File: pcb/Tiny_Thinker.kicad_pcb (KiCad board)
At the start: 2 copper layers, 47.9 x 46 mm, 35 parts, among them J1 USB_B_Micro, J2 SWD, J3 I2C1_A, J4 I2C1_B, J5 SPI1, J6 PWM_OUT, J7 ADC1, SW1 SW_Push, SW2 SW_SPDT, U1 STM32F446RET6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

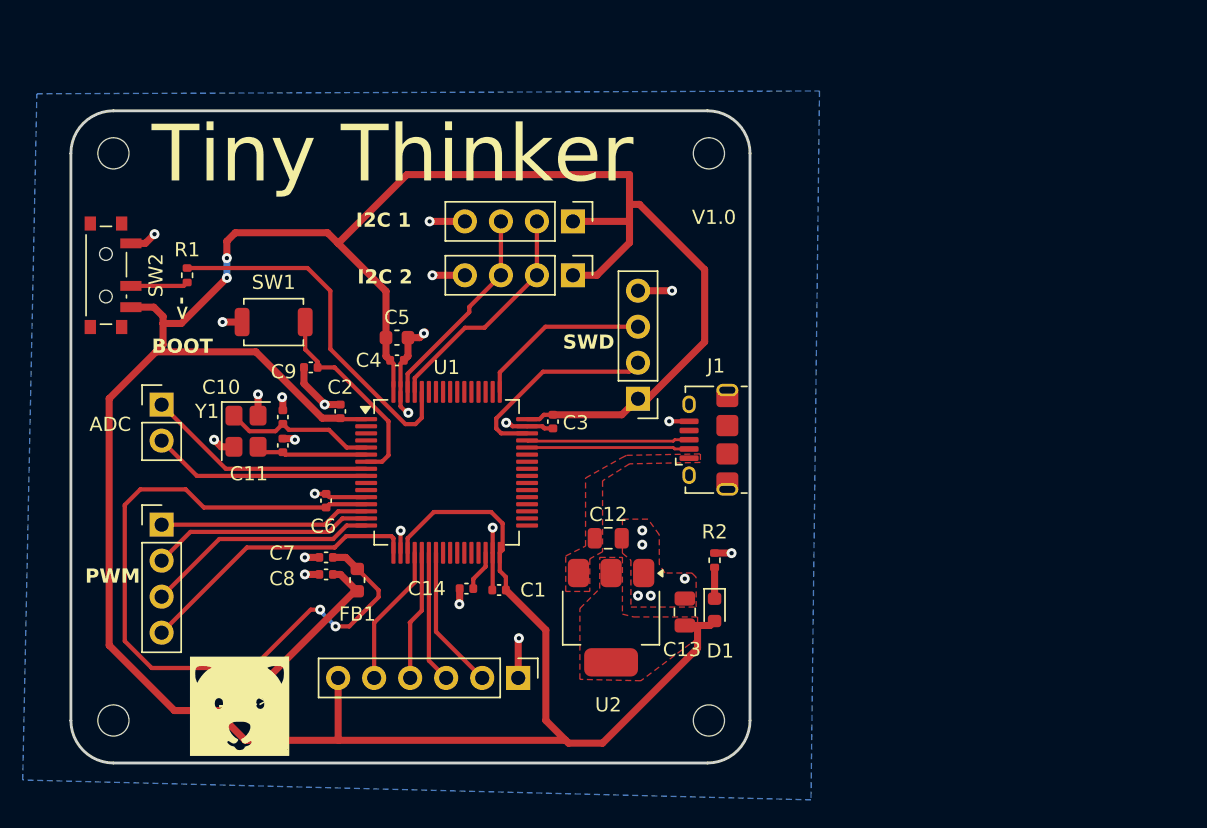
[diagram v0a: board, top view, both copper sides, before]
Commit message: added extra 100nf cap
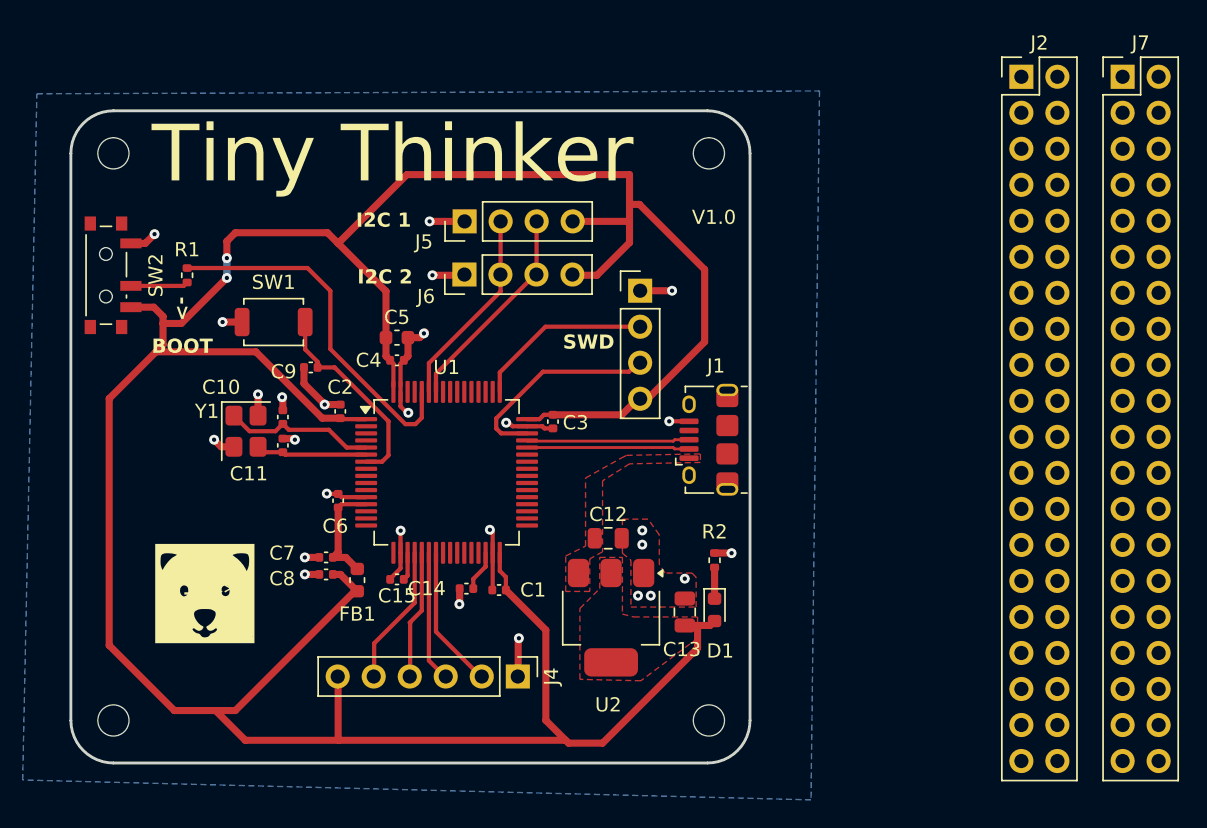
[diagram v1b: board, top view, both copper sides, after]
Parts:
- added C15: 100nF, Capacitor_SMD:C_0402_1005Metric, F.Cu at (105.0, 90.0)
- C1, C2, C3, C4, C9: value 100n -> 100nF
- C10, C11: value 10p -> 10pF
- C12, C13: value 22u -> 22uF
- C14: value 4.7u -> 4.7uF
- C5: value 10u -> 10uF
- C6: value 10n -> 10nF
- C7, C8: value 1u -> 1uF
- J2: value SWD -> Conn_02x20_Odd_Even; footprint Connector_PinHeader_2.54mm:PinHeader_1x04_P2.54mm_Vertical -> Connector_PinHeader_2.54mm:PinHeader_2x20_P2.54mm_Vertical
- J3: value I2C1_A -> SWD
- J4: value I2C1_B -> SPI1; footprint Connector_PinHeader_2.54mm:PinHeader_1x04_P2.54mm_Vertical -> Connector_PinHeader_2.54mm:PinHeader_1x06_P2.54mm_Vertical
- J5: value SPI1 -> I2C1_A; footprint Connector_PinHeader_2.54mm:PinHeader_1x06_P2.54mm_Vertical -> Connector_PinHeader_2.54mm:PinHeader_1x04_P2.54mm_Vertical
- J6: value PWM_OUT -> I2C1_B
- J7: value ADC1 -> Conn_02x20_Odd_Even; footprint Connector_PinHeader_2.54mm:PinHeader_1x02_P2.54mm_Vertical -> Connector_PinHeader_2.54mm:PinHeader_2x20_P2.54mm_Vertical
- moved J7 71.6 mm to (156.2, 54.6)
- moved J2 35.3 mm to (149.0, 54.6), turned to 0 degrees
- moved J5 32.4 mm to (109.8, 64.8), turned to 90 degrees
- moved J4 28.6 mm to (113.5, 96.9)
- moved J6 27.7 mm to (109.8, 68.5), turned to 90 degrees
- moved G*** 8.32 mm to (91.5, 91.0)
- moved J3 6.81 mm to (122.2, 69.7), turned to 0 degrees
- moved C6 0.85 mm to (100.8, 84.5)
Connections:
- J2 pad 1: +3.3V -> GND
- J2 pad 2: /SWDIO -> GND
- J2 pad 3: /SWCLK -> +3.3V
- J2 pad 4: GND -> +3.3V
- J3 pad 1: +3.3V -> GND
- J3 pad 2: /I2C1_SCL -> /SWCLK
- J3 pad 3: /I2C1_SDA -> /SWDIO
- J3 pad 4: GND -> +3.3V
- J4 pad 1: +3.3V -> GND
- J4 pad 2: /I2C1_SCL -> /SPI1_MOSI
- J4 pad 3: /I2C1_SDA -> /SPI1_MISO
- J4 pad 4: GND -> /SPI1_SCK
- J5 pad 2: /SPI1_MOSI -> /I2C1_SDA
- J5 pad 3: /SPI1_MISO -> /I2C1_SCL
- J5 pad 4: /SPI1_SCK -> +3.3V
- J6 pad 1: /PWM_1 -> GND
- J6 pad 2: /PWM_2 -> /I2C1_SDA
- J6 pad 3: /PWM_3 -> /I2C1_SCL
- J6 pad 4: /PWM_4 -> +3.3V
- J7 pad 1: /ADC_1 -> GND
- J7 pad 2: /ADC_2 -> GND
- U1 pad 10: unconnected-(U1-PC2-Pad10) -> /PC2
- U1 pad 11: unconnected-(U1-PC3-Pad11) -> /PC3
- U1 pad 14: /PWM_1 -> /PA0
- U1 pad 15: /PWM_2 -> /PA1
- U1 pad 16: /PWM_3 -> /PA2
- U1 pad 17: /PWM_4 -> /PA3
- U1 pad 2: unconnected-(U1-PC13-Pad2) -> /PC13
- U1 pad 24: unconnected-(U1-PC4-Pad24) -> /PC4
- U1 pad 25: unconnected-(U1-PC5-Pad25) -> /PC5
- U1 pad 26: unconnected-(U1-PB0-Pad26) -> /PB0
- U1 pad 27: unconnected-(U1-PB1-Pad27) -> /PB1
- U1 pad 28: unconnected-(U1-PB2-Pad28) -> /PB2
- U1 pad 29: unconnected-(U1-PB10-Pad29) -> /PB10
- U1 pad 3: unconnected-(U1-PC14-Pad3) -> /PC14
- U1 pad 33: unconnected-(U1-PB12-Pad33) -> /PB12
- U1 pad 34: unconnected-(U1-PB13-Pad34) -> /PB13
- U1 pad 35: unconnected-(U1-PB14-Pad35) -> /PB14
- U1 pad 36: unconnected-(U1-PB15-Pad36) -> /PB15
- U1 pad 37: unconnected-(U1-PC6-Pad37) -> /PC6
- U1 pad 38: unconnected-(U1-PC7-Pad38) -> /PC7
- U1 pad 39: unconnected-(U1-PC8-Pad39) -> /PC8
- U1 pad 4: unconnected-(U1-PC15-Pad4) -> /PC15
- U1 pad 40: unconnected-(U1-PC9-Pad40) -> /PC9
- U1 pad 41: unconnected-(U1-PA8-Pad41) -> /PA8
- U1 pad 42: unconnected-(U1-PA9-Pad42) -> /PA9
- U1 pad 43: unconnected-(U1-PA10-Pad43) -> /PA10
- U1 pad 50: unconnected-(U1-PA15-Pad50) -> /PA15
- U1 pad 51: unconnected-(U1-PC10-Pad51) -> /PC10
- U1 pad 52: unconnected-(U1-PC11-Pad52) -> /PC11
- U1 pad 53: unconnected-(U1-PC12-Pad53) -> /PC12
- U1 pad 54: unconnected-(U1-PD2-Pad54) -> /PD2
- U1 pad 55: unconnected-(U1-PB3-Pad55) -> /PB3
- U1 pad 56: unconnected-(U1-PB4-Pad56) -> /PB4
- U1 pad 57: unconnected-(U1-PB5-Pad57) -> /PB5
- U1 pad 58: unconnected-(U1-PB6-Pad58) -> /I2C1_SCL
- U1 pad 59: unconnected-(U1-PB7-Pad59) -> /I2C1_SDA
- U1 pad 61: /I2C1_SCL -> /PB8
- U1 pad 62: /I2C1_SDA -> /PB9
- U1 pad 8: /ADC_1 -> /PC0
- U1 pad 9: /ADC_2 -> /PC1
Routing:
- net +3.3VA: track 54.2 -> 7.80 mm, vias 2 -> 0
- net /PWM_4: track 20.3 -> 0.00 mm
- net /PWM_3: track 16.5 -> 0.00 mm
- net /ADC_1: track 16.3 -> 0.00 mm
- net /PWM_2: track 15.7 -> 0.00 mm
- net /ADC_2: track 15.5 -> 0.00 mm
- net /PWM_1: track 14.8 -> 0.00 mm
- net +3.3V: track 233.2 -> 224.2 mm
- net /I2C1_SCL: track 16.4 -> 15.0 mm
- net GND: track 48.3 -> 49.4 mm
- net /I2C1_SDA: track 14.8 -> 14.1 mm
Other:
- board text removed: "ADC"
- board text removed: "ADC 1"
- board text removed: "ADC 2"
- board text removed: "PWM"
- board text removed: "PWM 1"
- board text removed: "PWM 2"
- board text removed: "PWM 3"
- board text removed: "PWM 4"

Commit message: I honestly forgot what I did
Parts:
- moved C10 2.49 mm to (98.8, 80.3)
- moved C11 2.49 mm to (98.8, 82.3)
- moved Y1 2.49 mm to (96.2, 81.3)
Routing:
- net +3.3V: track 224.2 -> 228.0 mm, vias 2 -> 0
- net /HSE_IN: track 10.7 -> 8.14 mm
- net /HSE_OUT: track 7.85 -> 6.54 mm
- net GND: track 49.4 -> 48.7 mm, vias 27 -> 30
- net /BOOT0: vias 0 -> 2
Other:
- board text added: "I2C1 A"
- board text added: "I2C1 B"
- board text removed: "I2C 1"
- board text removed: "I2C 2"

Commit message: i dont even know
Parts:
- removed G***: LOGO, LOGO
- added R3: 4k7, Resistor_SMD:R_0402_1005Metric, F.Cu at (120.9, 81.9)
- added R4: 10k, Resistor_SMD:R_0402_1005Metric, F.Cu at (118.9, 82.2)
- moved J2 86.3 mm to (80.9, 107.5), turned to 90 degrees
- moved H4 76.3 mm to (155.2, 70.1)
- moved J7 74.5 mm to (81.7, 57.7), turned to 90 degrees
- moved H3 70.3 mm to (155.2, 64.2)
- moved J6 54.4 mm to (163.7, 75.4), turned to 0 degrees
- moved J5 50.5 mm to (159.1, 75.4), turned to 0 degrees
- moved H2 50.4 mm to (155.2, 58.2)
- moved H1 29.2 mm to (155.2, 52.3)
- moved J3 5.57 mm to (116.8, 71.2), turned to 90 degrees
- moved J4 2.09 mm to (114.0, 99.0)
- moved J1 1.50 mm to (125.5, 80.2)
- moved C1 0.80 mm to (112.2, 90.0)
- moved C14 0.70 mm to (109.9, 90.0)
- moved C3 0.41 mm to (115.8, 78.6)
- moved C12 0.40 mm to (119.5, 87.2)
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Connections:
- U1 pad 10: /PC2 -> /ADC1_IN12
- U1 pad 11: /PC3 -> /ADC1_IN13
- U1 pad 14: /PA0 -> unconnected-(U1-PA0-Pad14)
- U1 pad 15: /PA1 -> unconnected-(U1-PA1-Pad15)
- U1 pad 16: /PA2 -> unconnected-(U1-PA2-Pad16)
- U1 pad 17: /PA3 -> unconnected-(U1-PA3-Pad17)
- U1 pad 2: /PC13 -> unconnected-(U1-PC13-Pad2)
- U1 pad 24: /PC4 -> /ADC1_IN14
- U1 pad 25: /PC5 -> /ADC1_IN15
- U1 pad 26: /PB0 -> /ADC1_IN8
- U1 pad 27: /PB1 -> /ADC1_IN9
- U1 pad 28: /PB2 -> /TIM2_CH4
- U1 pad 29: /PB10 -> /TIM2_CH3
- U1 pad 3: /PC14 -> unconnected-(U1-PC14-Pad3)
- U1 pad 33: /PB12 -> unconnected-(U1-PB12-Pad33)
- U1 pad 34: /PB13 -> unconnected-(U1-PB13-Pad34)
- U1 pad 35: /PB14 -> unconnected-(U1-PB14-Pad35)
- U1 pad 36: /PB15 -> unconnected-(U1-PB15-Pad36)
- U1 pad 37: /PC6 -> unconnected-(U1-PC6-Pad37)
- U1 pad 38: /PC7 -> unconnected-(U1-PC7-Pad38)
- U1 pad 39: /PC8 -> /TIM3_CH3
- U1 pad 4: /PC15 -> unconnected-(U1-PC15-Pad4)
- U1 pad 40: /PC9 -> /TIM3_CH4
- U1 pad 41: /PA8 -> unconnected-(U1-PA8-Pad41)
- U1 pad 42: /PA9 -> /USB_VBUS
- U1 pad 43: /PA10 -> unconnected-(U1-PA10-Pad43)
- U1 pad 50: /PA15 -> /TIM2_CH1
- U1 pad 51: /PC10 -> unconnected-(U1-PC10-Pad51)
- U1 pad 52: /PC11 -> unconnected-(U1-PC11-Pad52)
- U1 pad 53: /PC12 -> unconnected-(U1-PC12-Pad53)
- U1 pad 54: /PD2 -> unconnected-(U1-PD2-Pad54)
- U1 pad 55: /PB3 -> /TIM2_CH2
- U1 pad 56: /PB4 -> /TIM3_CH1
- U1 pad 57: /PB5 -> /TIM3_CH2
- U1 pad 61: /PB8 -> /CAN1_RX
- U1 pad 62: /PB9 -> /CAN1_TX
- U1 pad 8: /PC0 -> /ADC1_IN10
- U1 pad 9: /PC1 -> /ADC1_IN11
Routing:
- net +3.3V: track 228.0 -> 204.0 mm
- net /I2C1_SCL: track 15.0 -> 0.00 mm
- net /I2C1_SDA: track 14.1 -> 0.00 mm
- net GND: track 48.7 -> 35.7 mm, vias 30 -> 26
- net /SPI1_MOSI: track 10.2 -> 0.00 mm
- net /SPI1_NSS: track 10.0 -> 0.00 mm
- net /SPI1_MISO: track 9.33 -> 0.00 mm
- net /SPI1_SCK: track 9.19 -> 0.00 mm
- net /USB_VBUS: track 0.00 -> 6.29 mm
- net /USB_D-: track 11.5 -> 9.69 mm
- net /USB_D+: track 11.5 -> 9.74 mm
- net /SWCLK: track 12.5 -> 11.0 mm
- net /SWDIO: track 14.6 -> 13.5 mm
- net /VCAP_1: track 2.89 -> 2.21 mm
- removed copper zone on B.Cu, net GND
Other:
- board outline removed
- board text removed: "+3.3V"
- board text removed: "GND"
- board text removed: "I2C1 A"
- board text removed: "I2C1 B"
- board text removed: "MISO"
- board text removed: "MOSI"
- board text removed: "NSS"
- board text removed: "SCK"
- board text removed: "SCL"
- board text removed: "SDA"
- board text removed: "SWCLK"
- board text removed: "SWD"
- board text removed: "SWDIO"
- board text removed: "Tiny Thinker"
- board text removed: "V1.0"

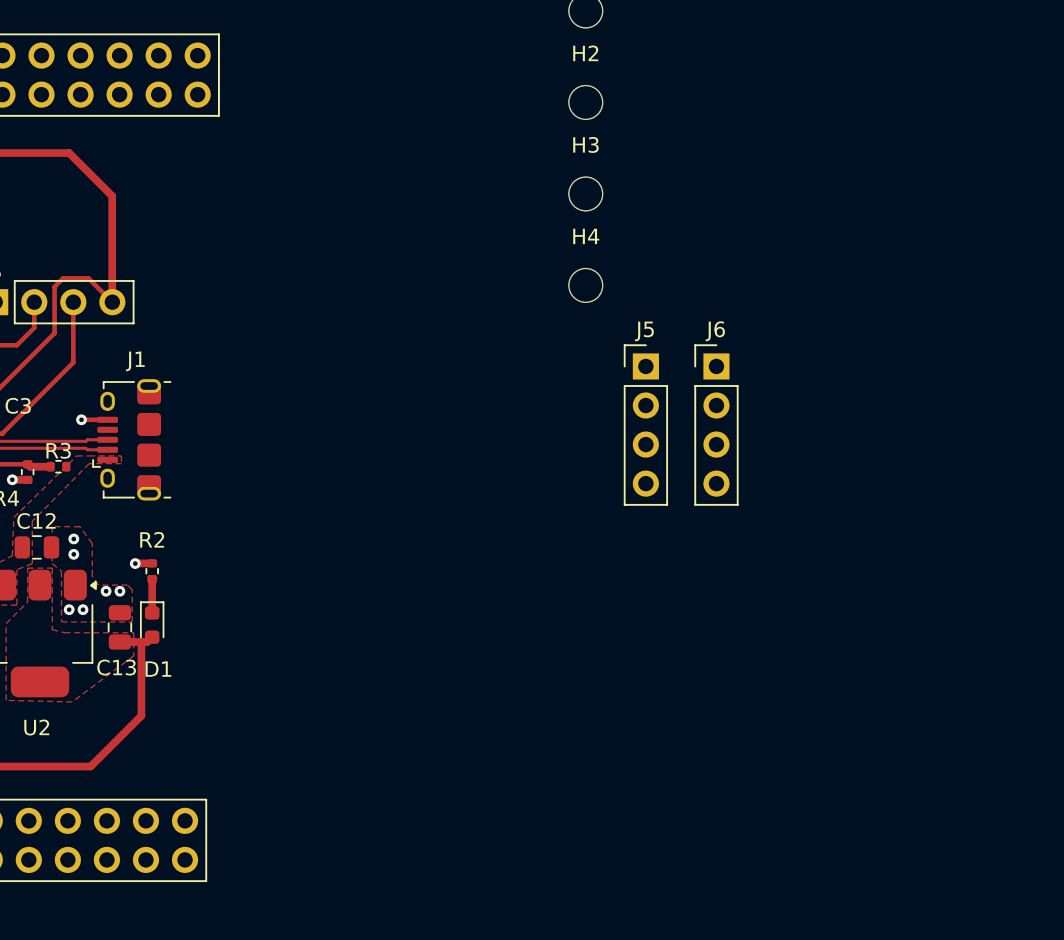
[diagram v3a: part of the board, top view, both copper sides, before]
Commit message: Added JLCPCB capabilities
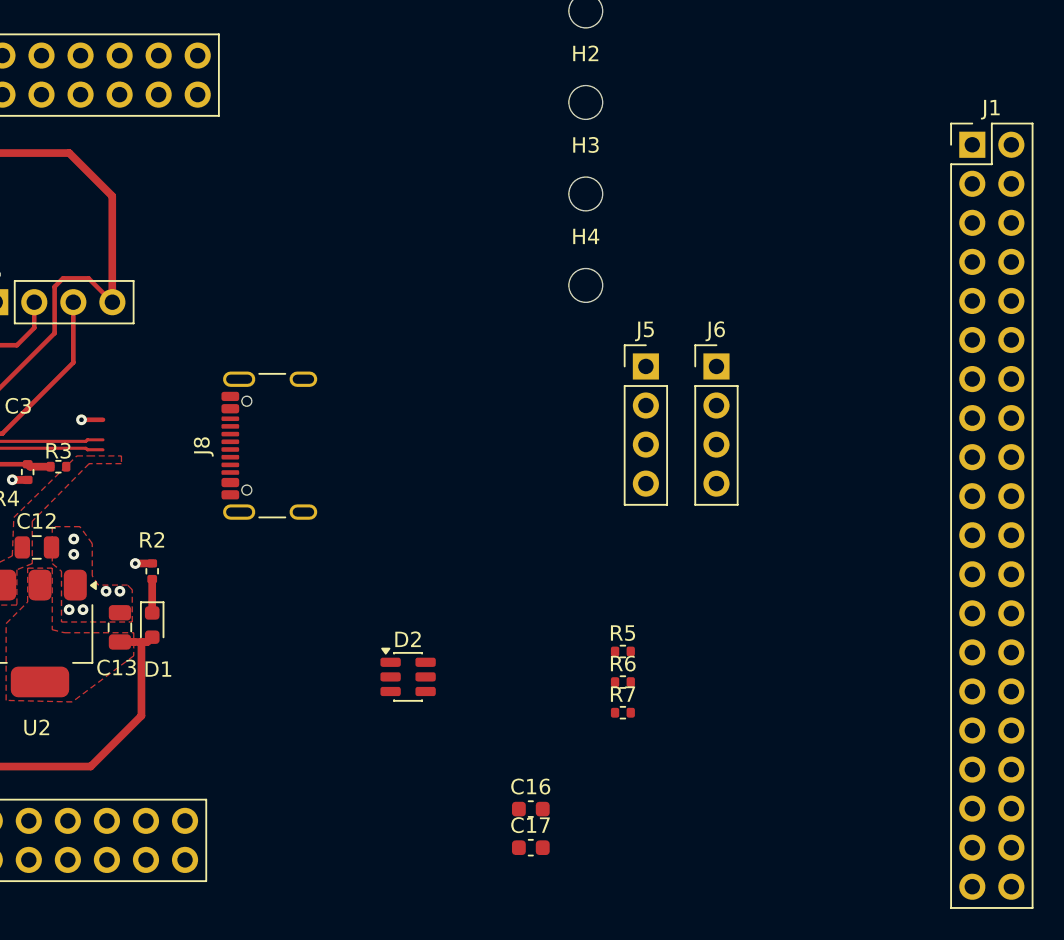
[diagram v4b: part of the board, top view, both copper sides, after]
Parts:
- added C16: 470nF, Capacitor_SMD:C_0603_1608Metric, F.Cu at (151.6, 104.2)
- added C17: 470nF, Capacitor_SMD:C_0603_1608Metric, F.Cu at (151.6, 106.7)
- added D2: USBLC6-2SC6, Package_TO_SOT_SMD:SOT-23-6, F.Cu at (143.6, 95.6)
- added J8: USB_C_Receptacle_USB2.0_16P, Connector_USB:USB_C_Receptacle_GCT_USB4105-xx-A_16P_TopMnt_Horizontal, F.Cu at (135.8, 80.5)
- added R5: 0R, Resistor_SMD:R_0402_1005Metric, F.Cu at (157.6, 93.9)
- added R6: 5k1, Resistor_SMD:R_0402_1005Metric, F.Cu at (157.6, 95.9)
- added R7: 5k1, Resistor_SMD:R_0402_1005Metric, F.Cu at (157.6, 97.9)
- FB1: value FerriteBead -> 120R
- J1: value USB_B_Micro -> Conn_02x20_Odd_Even; footprint Connector_USB:USB_Micro-B_Amphenol_10118194_Horizontal -> Connector_PinHeader_2.54mm:PinHeader_2x20_P2.54mm_Vertical
- moved J1 58.1 mm to (180.3, 61.0), turned to 0 degrees
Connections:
- C12 pad 1: VBUS -> +VBUSF
- J1 pad 1: VBUS -> +3.3V
- J1 pad 2: /USB_D- -> GND
- J1 pad 3: /USB_D+ -> GND
- J1 pad 4: unconnected-(J1-ID-Pad4) -> +3.3V
- J1 pad 5: GND -> unconnected-(J1-Pin_5-Pad5)
- J2 pad 1: GND -> +3.3V
- J2 pad 10: /PA3 -> unconnected-(J2-Pin_10-Pad10)
- J2 pad 11: GND -> unconnected-(J2-Pin_11-Pad11)
- J2 pad 12: GND -> unconnected-(J2-Pin_12-Pad12)
- J2 pad 13: /PA8 -> unconnected-(J2-Pin_13-Pad13)
- J2 pad 14: /PA9 -> GND
- J2 pad 15: /PA10 -> GND
- J2 pad 16: /PA15 -> unconnected-(J2-Pin_16-Pad16)
- J2 pad 17: GND -> unconnected-(J2-Pin_17-Pad17)
- J2 pad 18: GND -> unconnected-(J2-Pin_18-Pad18)
- J2 pad 19: /PB0 -> +3.3V
- J2 pad 20: /PB1 -> GND
- J2 pad 21: /PB2 -> GND
- J2 pad 22: /PB3 -> +3.3V
- J2 pad 23: GND -> unconnected-(J2-Pin_23-Pad23)
- J2 pad 24: GND -> unconnected-(J2-Pin_24-Pad24)
- J2 pad 25: /PB4 -> unconnected-(J2-Pin_25-Pad25)
- J2 pad 26: /PB5 -> GND
- J2 pad 27: /PB8 -> GND
- J2 pad 28: /PB9 -> unconnected-(J2-Pin_28-Pad28)
- J2 pad 29: GND -> unconnected-(J2-Pin_29-Pad29)
- J2 pad 3: +3.3V -> GND
- J2 pad 30: GND -> unconnected-(J2-Pin_30-Pad30)
- J2 pad 31: /PB10 -> unconnected-(J2-Pin_31-Pad31)
- J2 pad 32: /PB12 -> GND
- J2 pad 33: /PB13 -> GND
- J2 pad 34: /PB14 -> unconnected-(J2-Pin_34-Pad34)
- J2 pad 35: GND -> unconnected-(J2-Pin_35-Pad35)
- J2 pad 36: GND -> unconnected-(J2-Pin_36-Pad36)
- J2 pad 37: GND -> +3.3V
- J2 pad 39: +3.3V -> GND
- J2 pad 5: GND -> unconnected-(J2-Pin_5-Pad5)
- J2 pad 6: GND -> unconnected-(J2-Pin_6-Pad6)
- J2 pad 7: /PA0 -> unconnected-(J2-Pin_7-Pad7)
- J2 pad 8: /PA1 -> GND
- J2 pad 9: /PA2 -> GND
- R3 pad 1: VBUS -> +VBUSF
- U1 pad 14: unconnected-(U1-PA0-Pad14) -> /TIM2_CH1
- U1 pad 15: unconnected-(U1-PA1-Pad15) -> /TIM2_CH2
- U1 pad 16: unconnected-(U1-PA2-Pad16) -> /TIM2_CH3
- U1 pad 17: unconnected-(U1-PA3-Pad17) -> /TIM2_CH4
- U1 pad 28: /TIM2_CH4 -> unconnected-(U1-PB2-Pad28)
- U1 pad 29: /TIM2_CH3 -> unconnected-(U1-PB10-Pad29)
- U1 pad 50: /TIM2_CH1 -> unconnected-(U1-PA15-Pad50)
- U1 pad 55: /TIM2_CH2 -> unconnected-(U1-PB3-Pad55)
- U2 pad 3: VBUS -> +VBUSF
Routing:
- added copper zone on F.Cu, net +VBUSF
- removed copper zone on F.Cu, net VBUS
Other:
- copper layers 2 -> 4
- rule pad_to_mask_clearance: 0 -> 0.1

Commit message: checkpoint
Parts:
- added FM1: Fiducial, Fiducial:Fiducial_1mm_Mask2mm, F.Cu at (205.0, 90.9)
- added FM2: Fiducial, Fiducial:Fiducial_1mm_Mask2mm, F.Cu at (205.0, 94.5)
- added FM3: Fiducial, Fiducial:Fiducial_1mm_Mask2mm, F.Cu at (205.0, 98.0)
- moved C10 3.33 mm to (95.5, 79.8)
- moved C11 3.33 mm to (95.5, 81.8)
- moved Y1 3.33 mm to (92.9, 80.8)
- moved C1 0.58 mm to (112.8, 90.0)
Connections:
- U1 pad 37: unconnected-(U1-PC6-Pad37) -> /TIM3_CH1
- U1 pad 38: unconnected-(U1-PC7-Pad38) -> /TIM3_CH2
- U1 pad 56: /TIM3_CH1 -> unconnected-(U1-PB4-Pad56)
- U1 pad 57: /TIM3_CH2 -> unconnected-(U1-PB5-Pad57)
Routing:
- net +3.3V: track 204.0 -> 20.0 mm
- net /HSE_OUT: track 6.54 -> 1.91 mm
- net /HSE_IN: track 8.14 -> 4.14 mm
- net GND: track 35.7 -> 34.9 mm, vias 26 -> 25
- net /BOOT0: vias 2 -> 0
- added copper zone on In1.Cu, net GND
- added copper zone on In2.Cu, net GND
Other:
- board outline added: 118.9 x 69.3 mm
